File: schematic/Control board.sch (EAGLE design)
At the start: 10 parts, among them IC1 TPS62173

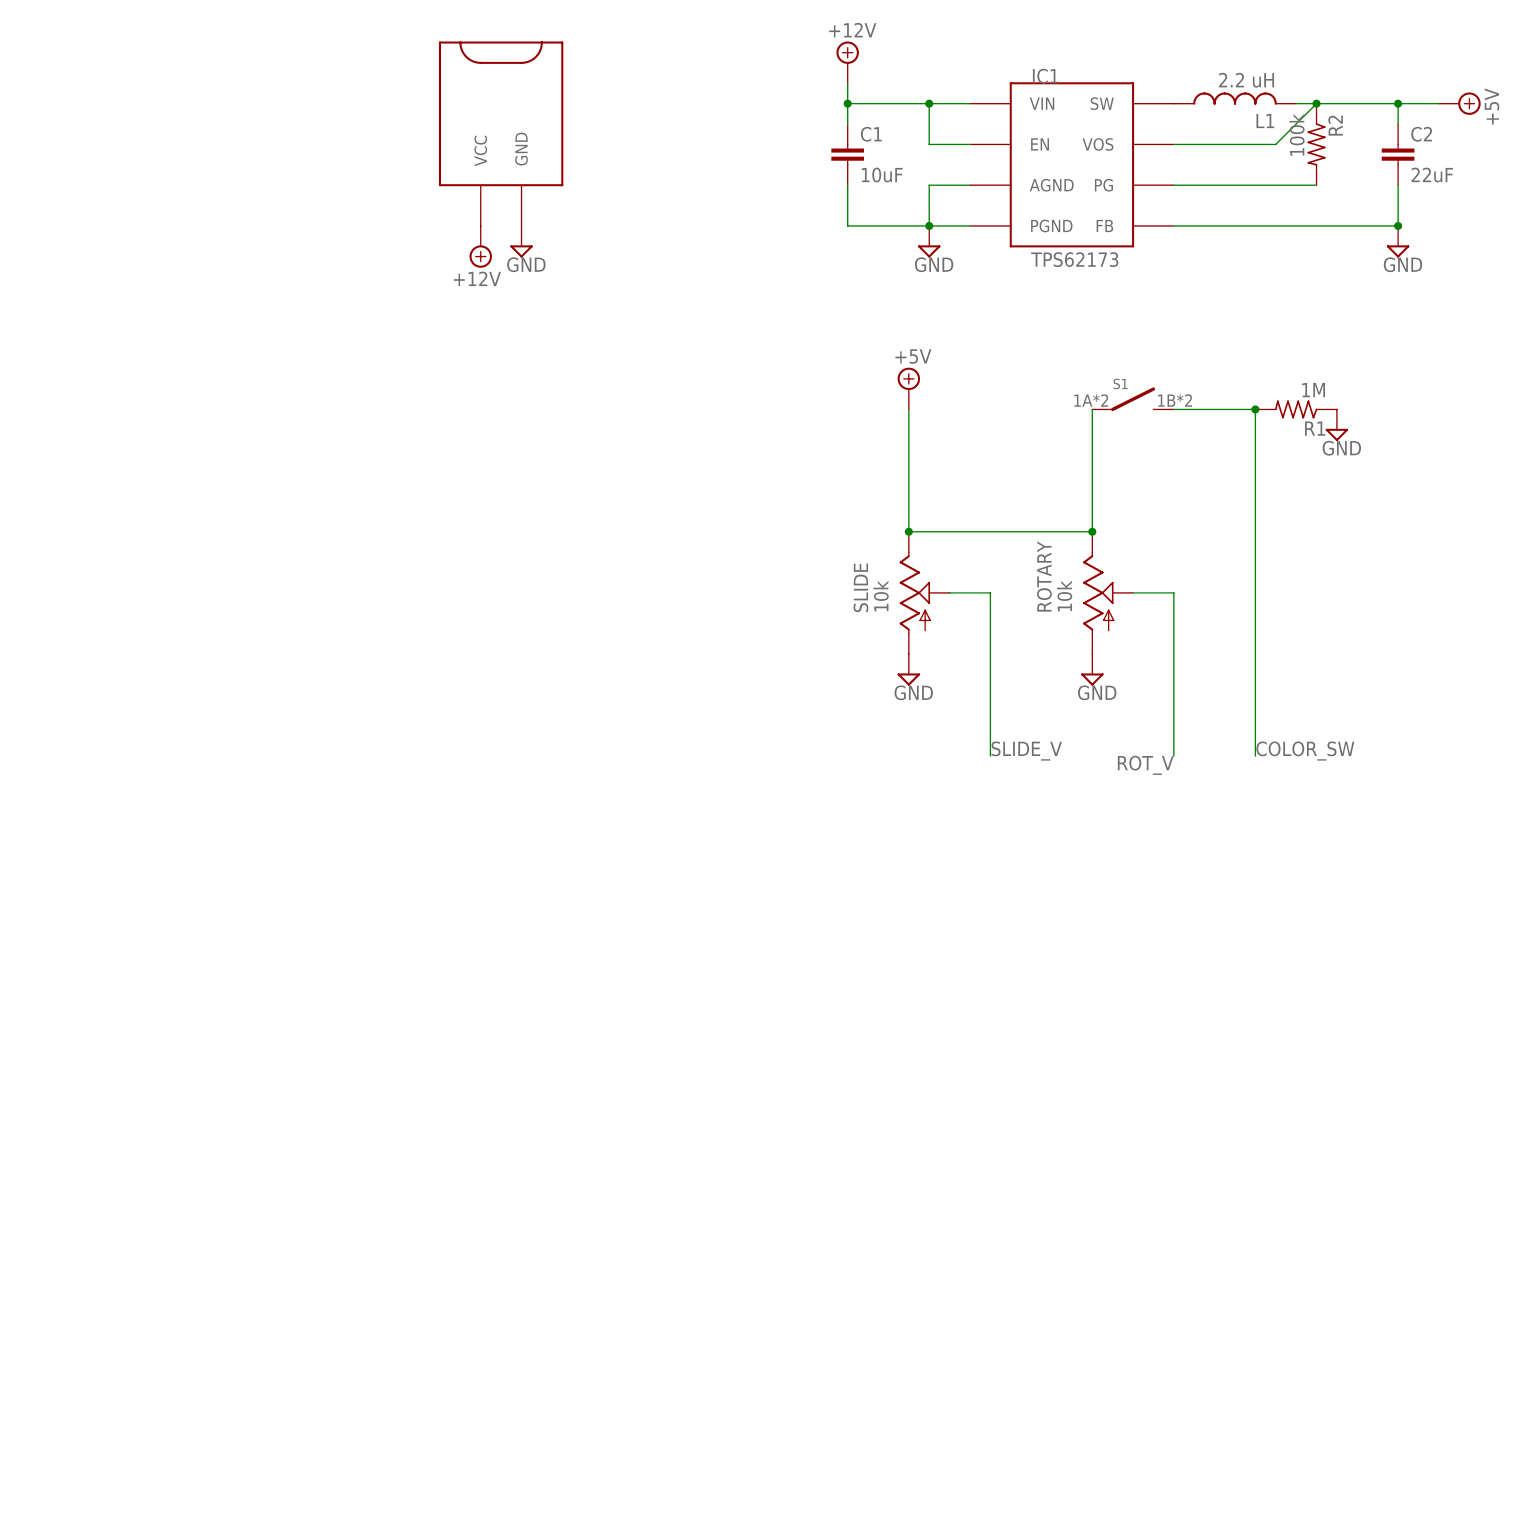
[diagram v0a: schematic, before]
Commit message: Added more library components and updated the board design
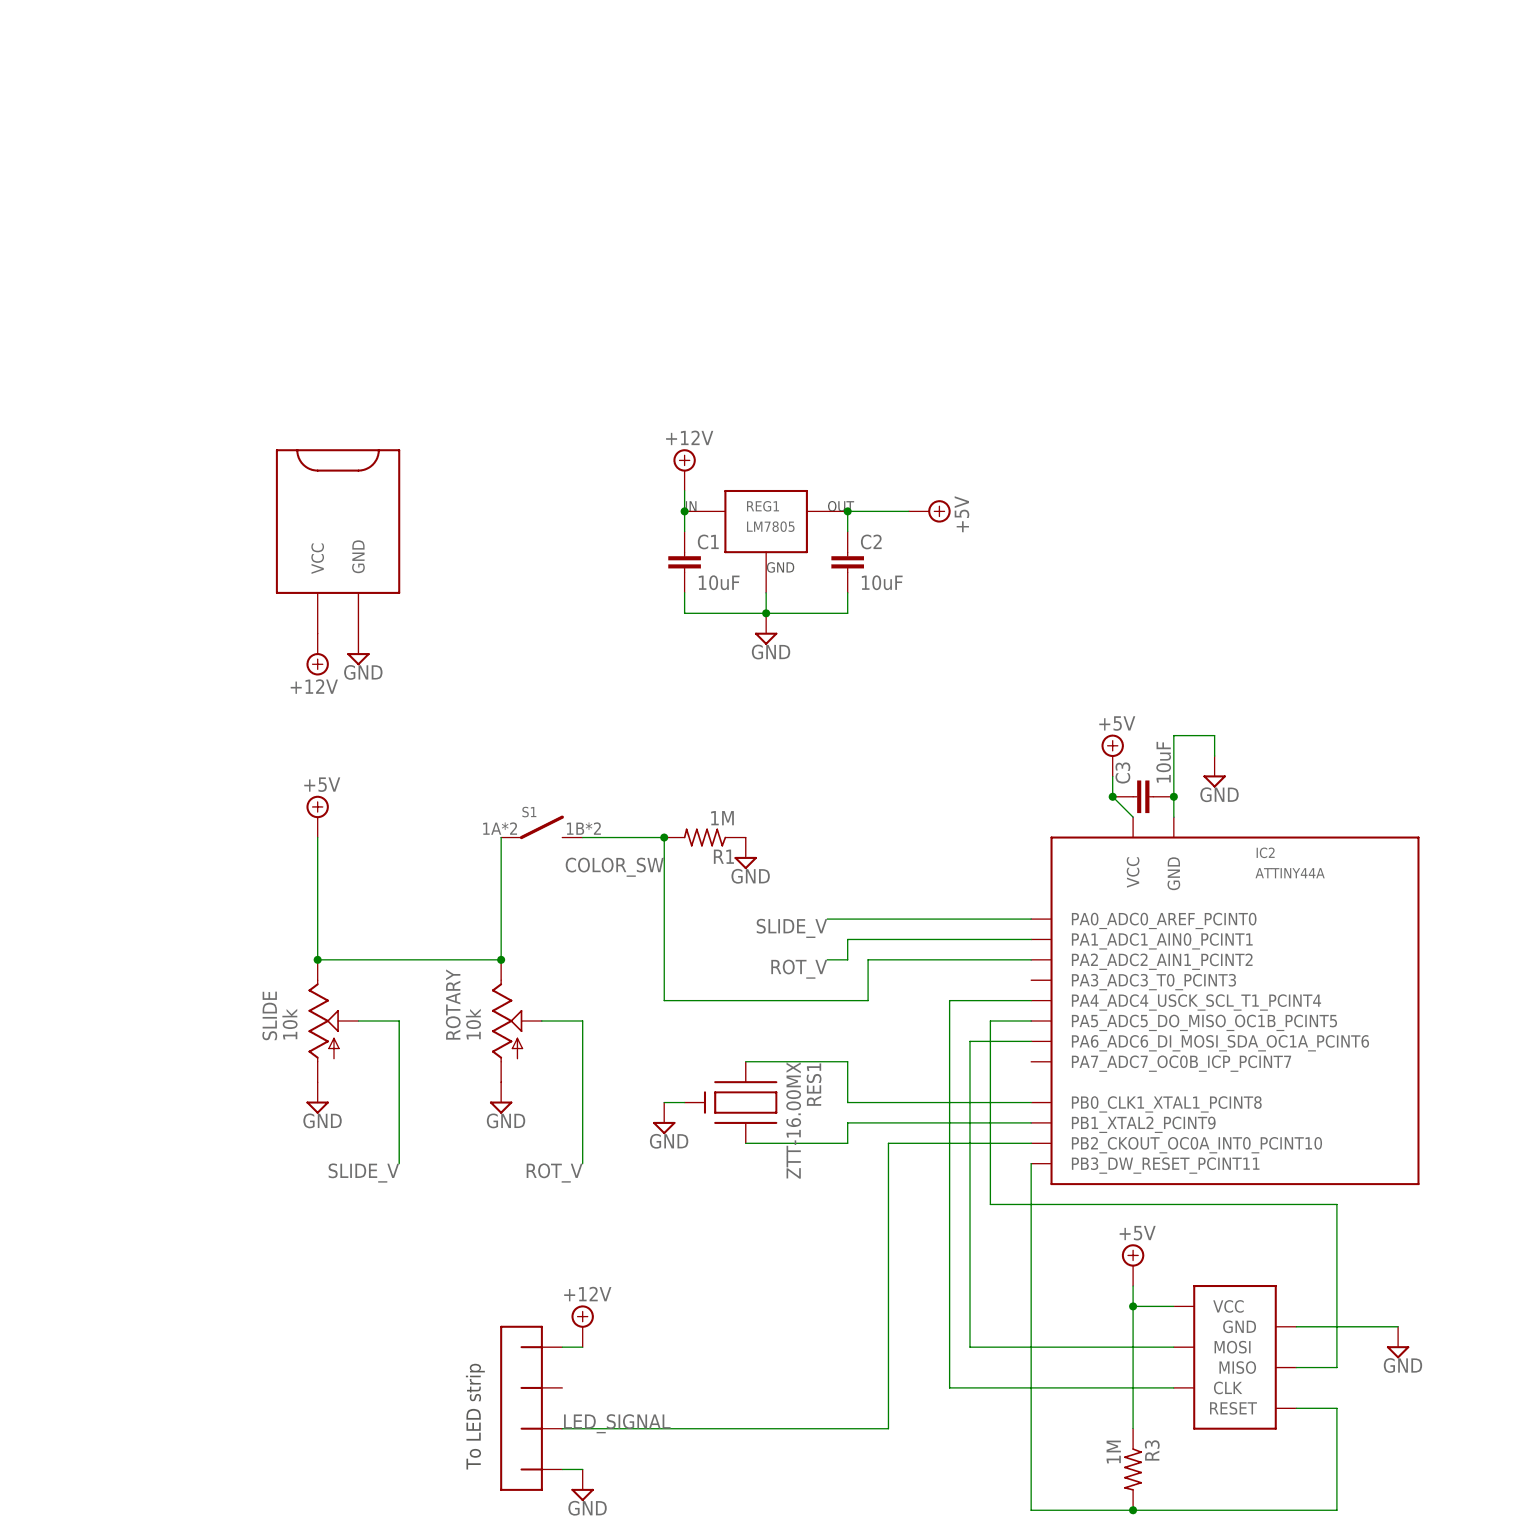
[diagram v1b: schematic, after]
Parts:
- removed IC1: TPS62173, RGB LED project:TPS62173
- removed L1: 2.2 uH, RGB LED project:L_US
- removed R2: 100k, resistor:R-US_R0402
- added C3: 10uF, resistor:C-EUC0603
- added CONN1: 4-PIN-RIGHT-ANGLE, RGB LED project:4-PIN-RIGHT-ANGLE
- added IC2: ATTINY44A, RGB LED project:ATTINY44A
- added R3: 1M, resistor:R-US_0207/7
- added REG1: LM7805, RGB LED project:LM7805
- added RES1: ZTT-16.00MX, RGB LED project:ZTT-16.00MX
- added U$1: ISP, RGB LED project:ISP
- C2: value 22uF -> 10uF
- R1: device resistor:R-US_R0402 -> resistor:R-US_0207/7
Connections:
- removed net N$1: IC1.SW, L1.1
- removed net N$3: IC1.PG, R2.2
- new net LED_SIGNAL: CONN1.P$2, IC2.PB2_CKOUT_OC0A_INT0_PCINT10
- new net MISO: IC2.PA5_ADC5_DO_MISO_OC1B_PCINT5, U$1.MISO
- new net MOSI: IC2.PA6_ADC6_DI_MOSI_SDA_OC1A_PCINT6, U$1.MOSI
- new net N$2: IC2.PB0_CLK1_XTAL1_PCINT8, RES1.X1
- new net N$4: IC2.PB1_XTAL2_PCINT9, RES1.X2
- new net RESET: IC2.PB3_DW_RESET_PCINT11, R3.2, U$1.RESET
- new net SCK: IC2.PA4_ADC4_USCK_SCL_T1_PCINT4, U$1.CLK
- net +12V: now also CONN1.P$4, REG1.IN; no longer IC1.EN, IC1.VIN
- net +5V: now also C3.1, IC2.VCC, R3.1, REG1.OUT, U$1.VCC; no longer IC1.VOS, L1.2, R2.1
- net COLOR_SW: now also IC2.PA2_ADC2_AIN1_PCINT2
- net GND: now also C3.2, CONN1.P$1, IC2.GND, REG1.GND, RES1.GND, U$1.GND; no longer IC1.AGND, IC1.FB, IC1.PGND
- net ROT_V: now also IC2.PA1_ADC1_AIN0_PCINT1
- net SLIDE_V: now also IC2.PA0_ADC0_AREF_PCINT0
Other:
- note added: "To LED strip"
- moved on the sheet: C1, C2, R1, ROTARY, S1, SLIDE

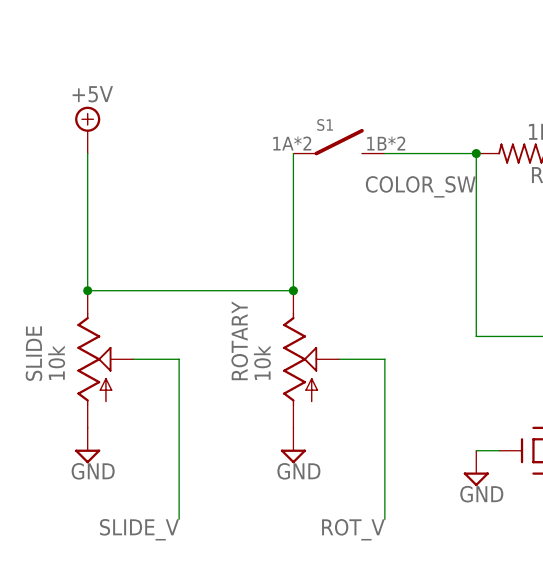
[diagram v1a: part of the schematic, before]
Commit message: Updated schematic, board file, and library; also updated the 3D model
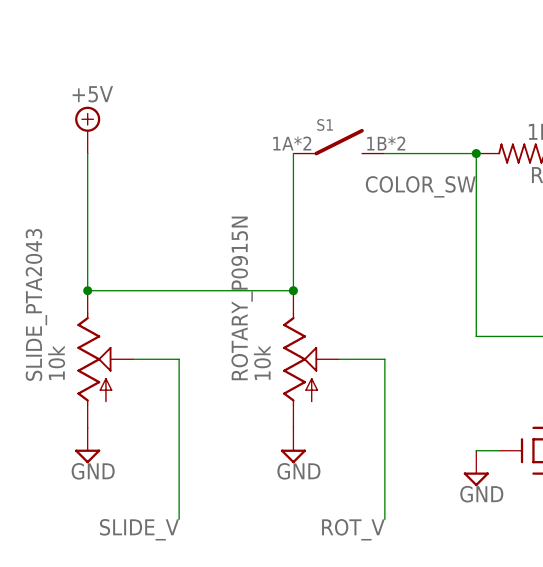
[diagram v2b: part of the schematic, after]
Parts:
- renumbered ROTARY to ROTARY_P0915N, SLIDE to SLIDE_PTA2043
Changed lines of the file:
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@@
 <parts>
 <part name="S1" library="RGB LED project" deviceset="D6R00" device=""/>
-<part name="ROTARY" library="RGB LED project" deviceset="P0915N" device="" value="10k"/>
-<part name="SLIDE" library="RGB LED project" deviceset="PTA2043" device="" value="10k"/>
+<part name="ROTARY_P0915N" library="RGB LED project" deviceset="P0915N" device="" value="10k"/>
+<part name="SLIDE_PTA2043" library="RGB LED project" deviceset="PTA2043" device="" value="10k"/>
 <part name="SUPPLY1" library="supply2" deviceset="+5V" device=""/>
 <part name="SUPPLY2" library="supply2" deviceset="GND" device=""/>
@@
 <instances>
 <instance part="S1" gate="G$1" x="-35.56" y="-7.62"/>
-<instance part="ROTARY" gate="G$1" x="-38.1" y="-30.48"/>
-<instance part="SLIDE" gate="G$1" x="-60.96" y="-30.48"/>
+<instance part="ROTARY_P0915N" gate="G$1" x="-38.1" y="-30.48"/>
+<instance part="SLIDE_PTA2043" gate="G$1" x="-60.96" y="-30.48"/>
 <instance part="SUPPLY1" gate="+5V" x="-60.96" y="-5.08"/>
 <instance part="SUPPLY2" gate="GND" x="-60.96" y="-40.64"/>
@@
 <segment>
 <pinref part="SUPPLY1" gate="+5V" pin="+5V"/>
-<pinref part="SLIDE" gate="G$1" pin="B"/>
+<pinref part="SLIDE_PTA2043" gate="G$1" pin="B"/>
 <wire x1="-60.96" y1="-7.62" x2="-60.96" y2="-22.86" width="0.1524" layer="91"/>
-<pinref part="ROTARY" gate="G$1" pin="B"/>
+<pinref part="ROTARY_P0915N" gate="G$1" pin="B"/>
 <wire x1="-60.96" y1="-22.86" x2="-38.1" y2="-22.86" width="0.1524" layer="91"/>
 <pinref part="S1" gate="G$1" pin="P$1"/>
@@
 <net name="SLIDE_V" class="0">
 <segment>
-<pinref part="SLIDE" gate="G$1" pin="S"/>
+<pinref part="SLIDE_PTA2043" gate="G$1" pin="S"/>
 <wire x1="-55.88" y1="-30.48" x2="-50.8" y2="-30.48" width="0.1524" layer="91"/>
 <wire x1="-50.8" y1="-30.48" x2="-50.8" y2="-48.26" width="0.1524" layer="91"/>
@@
 <net name="ROT_V" class="0">
 <segment>
-<pinref part="ROTARY" gate="G$1" pin="S"/>
+<pinref part="ROTARY_P0915N" gate="G$1" pin="S"/>
 <wire x1="-33.02" y1="-30.48" x2="-27.94" y2="-30.48" width="0.1524" layer="91"/>
 <wire x1="-27.94" y1="-30.48" x2="-27.94" y2="-48.26" width="0.1524" layer="91"/>
@@
 <net name="GND" class="0">
 <segment>
-<pinref part="SLIDE" gate="G$1" pin="A"/>
+<pinref part="SLIDE_PTA2043" gate="G$1" pin="A"/>
 <pinref part="SUPPLY2" gate="GND" pin="GND"/>
 </segment>
 <segment>
-<pinref part="ROTARY" gate="G$1" pin="A"/>
+<pinref part="ROTARY_P0915N" gate="G$1" pin="A"/>
 <pinref part="SUPPLY3" gate="GND" pin="GND"/>
 </segment>
